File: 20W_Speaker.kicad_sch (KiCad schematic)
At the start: 24 parts, among them J1 Conn_01x02, J2 Conn_01x02, J3 Conn_01x02, J4 Conn_01x02, U1 PAM8320RDR

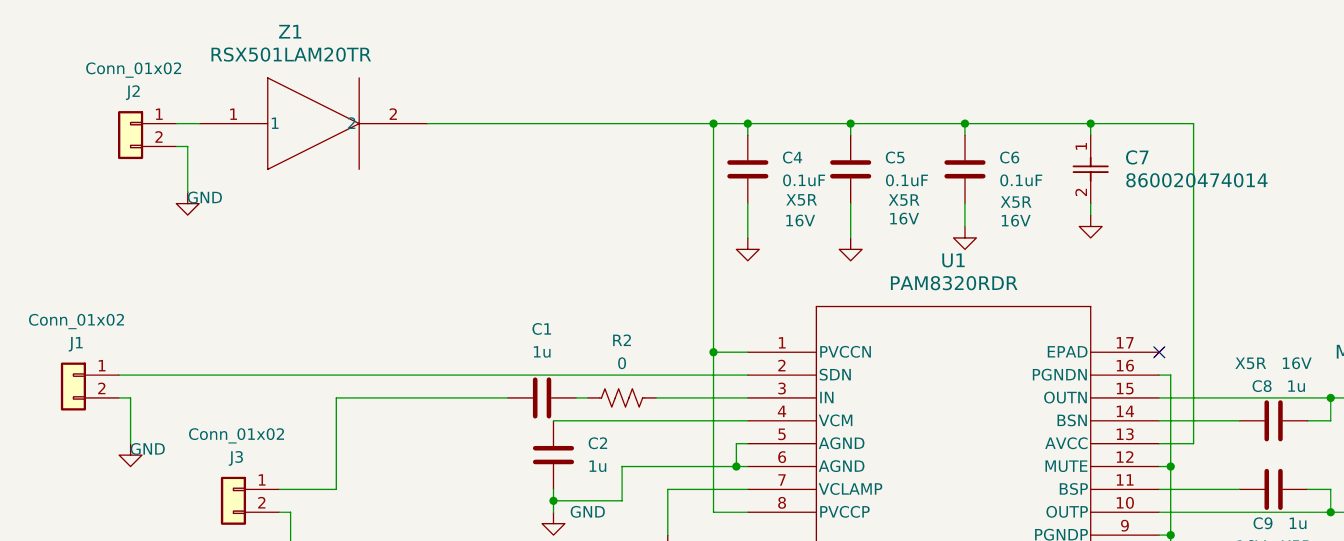
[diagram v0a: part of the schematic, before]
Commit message: PCB submitted for order
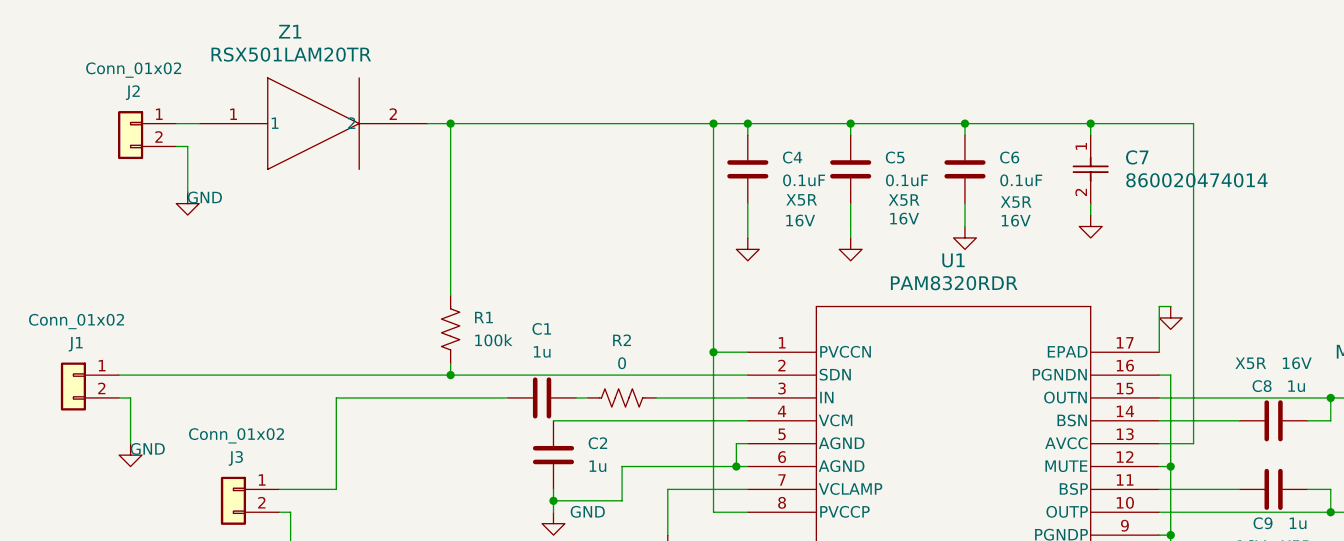
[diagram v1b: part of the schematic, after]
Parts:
- added R1: 100k, Resistor_SMD:R_0603_1608Metric, symbol Device:R_US
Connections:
- net GND: now also U1.17 (EPAD)
- net at C4.1, C5.1, C6.1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: now also R1.1
- net at J1.1 (Pin_1), U1.2 (SDN): now also R1.2
- no-connect marks 1 -> 0
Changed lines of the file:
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@@
   (junction (at 120.65 80.01) (diameter 0) (color 0 0 0 0)
   )
+  (junction (at 91.44 54.61) (diameter 0) (color 0 0 0 0)
+  )
   (junction (at 189.23 85.09) (diameter 0) (color 0 0 0 0)
   )
   (junction (at 124.46 54.61) (diameter 0) (color 0 0 0 0)
   )
+  (junction (at 91.44 82.55) (diameter 0) (color 0 0 0 0)
+  )
   (junction (at 171.45 92.71) (diameter 0) (color 0 0 0 0)
   )
@@
   (junction (at 162.56 54.61) (diameter 0) (color 0 0 0 0)
   )
-  (no_connect (at 170.18 80.01))
   (wire (pts (xy 189.23 95.25) (xy 189.23 97.79))
     (stroke (width 0) (type default))
   )
-  (wire (pts (xy 120.65 54.61) (xy 88.9 54.61))
+  (wire (pts (xy 120.65 54.61) (xy 91.44 54.61))
     (stroke (width 0) (type default))
   )
@@
     (stroke (width 0) (type default))
   )
+  (wire (pts (xy 91.44 54.61) (xy 88.9 54.61))
+    (stroke (width 0) (type default))
+  )
   (wire (pts (xy 170.18 92.71) (xy 171.45 92.71))
     (stroke (width 0) (type default))
@@
     (stroke (width 0) (type default))
   )
+  (wire (pts (xy 91.44 82.55) (xy 124.46 82.55))
+    (stroke (width 0) (type default))
+  )
   (wire (pts (xy 222.25 97.79) (xy 222.25 104.14))
     (stroke (width 0) (type default))
@@
     (stroke (width 0) (type default))
   )
+  (wire (pts (xy 91.44 54.61) (xy 91.44 73.66))
+    (stroke (width 0) (type default))
+  )
   (wire (pts (xy 120.65 80.01) (xy 124.46 80.01))
     (stroke (width 0) (type default))
@@
     (stroke (width 0) (type default))
   )
+  (wire (pts (xy 171.45 74.93) (xy 170.18 74.93))
+    (stroke (width 0) (type default))
+  )
   (wire (pts (xy 222.25 97.79) (xy 236.22 97.79))
     (stroke (width 0) (type default))
@@
     (stroke (width 0) (type default))
   )
+  (wire (pts (xy 170.18 74.93) (xy 170.18 80.01))
+    (stroke (width 0) (type default))
+  )
   (wire (pts (xy 120.65 54.61) (xy 120.65 80.01))
     (stroke (width 0) (type default))
@@
     (stroke (width 0) (type default))
   )
+  (wire (pts (xy 91.44 81.28) (xy 91.44 82.55))
+    (stroke (width 0) (type default))
+  )
   (wire (pts (xy 170.18 90.17) (xy 173.99 90.17))
     (stroke (width 0) (type default))
@@
     (stroke (width 0) (type default))
   )
-  (wire (pts (xy 54.61 82.55) (xy 124.46 82.55))
+  (wire (pts (xy 54.61 82.55) (xy 91.44 82.55))
     (stroke (width 0) (type default))
   )
@@
     )
   )
+  (symbol (lib_id "power:GND") (at 171.45 74.93 0) (unit 1)
+    (in_bom yes) (on_board yes) (dnp no)
+    (property "Reference" "#PWR017" (at 171.45 81.28 0)
+      (effects (font (size 1.27 1.27)) hide)
+    )
+    (property "Value" "GND" (at 168.91 74.93 0)
+      (effects (font (size 1.27 1.27)) hide)
+    )
+    (property "Footprint" "" (at 171.45 74.93 0)
+      (effects (font (size 1.27 1.27)) hide)
+    )
+    (property "Datasheet" "" (at 171.45 74.93 0)
+      (effects (font (size 1.27 1.27)) hide)
+    )
+    (pin "1")
+    (instances
+      (project "20W_Speaker"
+        (path "/a09edeed-43df-4523-a026-79a5a11a7974"
+          (reference "#PWR017") (unit 1)
+        )
+      )
+      (project "DaisySeedBreakout"
+        (path "/a83c9f4b-f61b-47d4-b39d-4636bff6eb0e"
+          (reference "#PWR021") (unit 1)
+        )
+        (path "/a83c9f4b-f61b-47d4-b39d-4636bff6eb0e/b269dd26-915f-458b-a2d7-e1fbc9f1daa5"
+          (reference "#PWR071") (unit 1)
+        )
+      )
+      (project "DaisySeedAccessories"
+        (path "/f4e212fd-fab8-40de-a317-91335511a529/0f60a6ff-7540-465b-9f59-804e6fc8018e"
+          (reference "#PWR037") (unit 1)
+        )
+      )
+    )
+  )
   (symbol (lib_id "Device:R_US") (at 236.22 107.95 0) (unit 1)
     (in_bom yes) (on_board yes) (dnp no) (fields_autoplaced)
@@
         )
       )
+    )
+  )
+  (symbol (lib_id "Device:R_US") (at 91.44 77.47 0) (unit 1)
+    (in_bom yes) (on_board yes) (dnp no) (fields_autoplaced)
+    (property "Reference" "R1" (at 93.98 76.2 0)
+      (effects (font (size 1.27 1.27)) (justify left))
+    )
+    (property "Value" "100k" (at 93.98 78.74 0)
+      (effects (font (size 1.27 1.27)) (justify left))
+    )
+    (property "Footprint" "Resistor_SMD:R_0603_1608Metric" (at 92.456 77.724 90)
+      (effects (font (size 1.27 1.27)) hide)
+    )
+    (property "Datasheet" "~" (at 91.44 77.47 0)
+      (effects (font (size 1.27 1.27)) hide)
+    )
+    (pin "1")
+    (pin "2")
+    (instances
+      (project "20W_Speaker"
+        (path "/a09edeed-43df-4523-a026-79a5a11a7974"
+          (reference "R1") (unit 1)
+        )
+      )
+      (project "DaisySeedBreakout"
+        (path "/a83c9f4b-f61b-47d4-b39d-4636bff6eb0e"
+          (reference "R8") (unit 1)
+        )
+        (path "/a83c9f4b-f61b-47d4-b39d-4636bff6eb0e/a0f8a1fd-6189-4b02-8cf7-e8d7538f4e50"
+          (reference "R23") (unit 1)
+        )
+        (path "/a83c9f4b-f61b-47d4-b39d-4636bff6eb0e/b269dd26-915f-458b-a2d7-e1fbc9f1daa5"
+          (reference "R58") (unit 1)
+        )
+      )
+      (project "DaisySeedAccessories"
+        (path "/f4e212fd-fab8-40de-a317-91335511a529/0f60a6ff-7540-465b-9f59-804e6fc8018e"
+          (reference "R27") (unit 1)
+        )
+      )
